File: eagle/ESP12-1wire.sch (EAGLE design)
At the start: 15 parts, among them IC1 LF33CDT, J1 22-05-7038-03, J2 22-05-7038-03, J3 22-05-7038-03, J4 22-05-7048-04

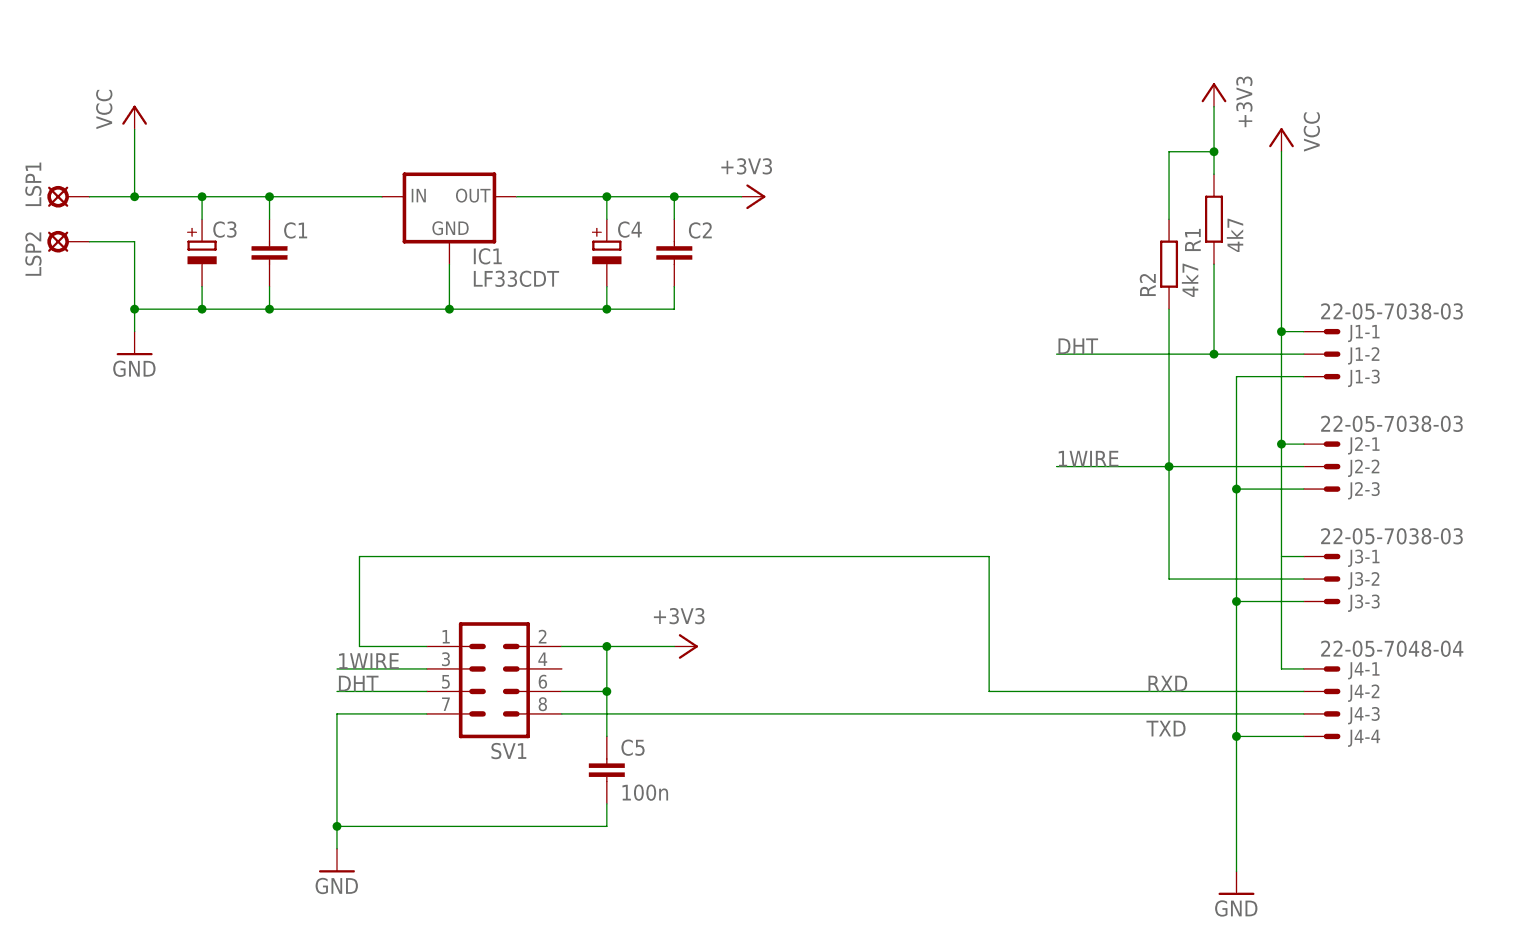
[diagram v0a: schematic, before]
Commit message: new version with ESP-12 module
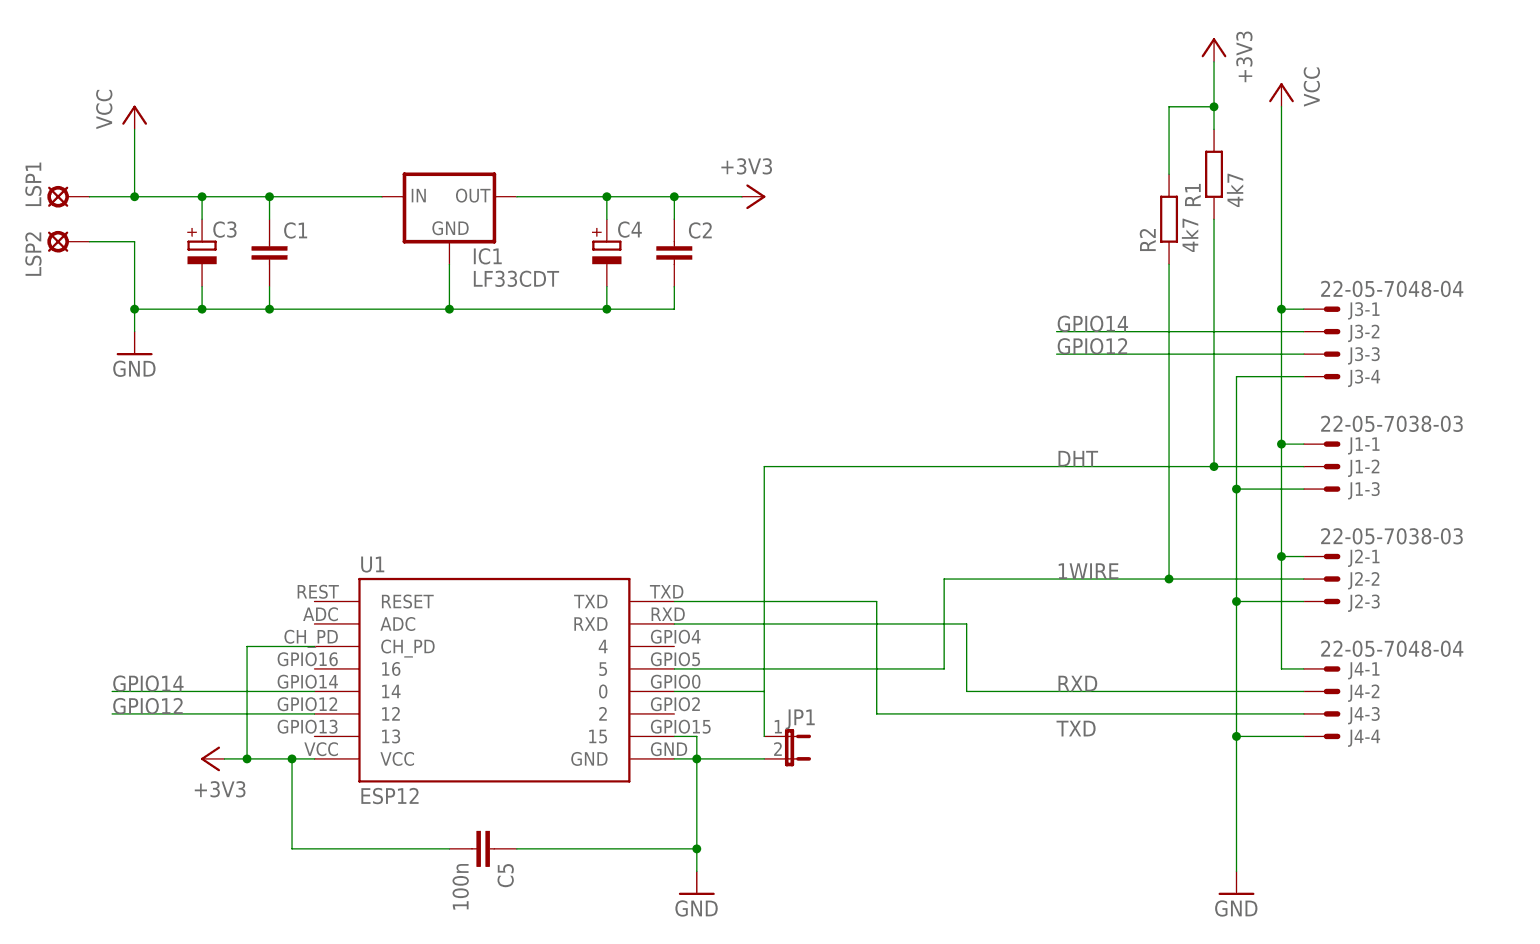
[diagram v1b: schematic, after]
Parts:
- removed SV1: (no value), con-lstb:MA04-2
- added JP1: (no value), jumper:JP1E
- added U1: ESP12, ESP:ESP12
- J3: value 22-05-7038-03 -> 22-05-7048-04; device con-molex:22-05-7038-03 -> con-molex:22-05-7048-04
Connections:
- new net GPIO12: J3-3.S, U1.12
- new net GPIO14: J3-2.S, U1.14
- net +3V3: now also C5.2, U1.CH_PD, U1.VCC; no longer C5.1, SV1.2, SV1.6
- net 1WIRE: now also U1.5; no longer J3-2.S, SV1.3
- net DHT: now also JP1.1, U1.0; no longer SV1.5
- net GND: now also C5.1, J3-4.S, JP1.2, U1.15, U1.GND; no longer C5.2, J3-3.S, SV1.7
- net RXD: now also U1.RXD; no longer SV1.1
- net TXD: now also U1.TXD; no longer SV1.8
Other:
- moved on the sheet: C5, J1-1, J1-2, J1-3, J2-1, J2-2, J2-3, J3-1, J3-2, J3-3, R1, R2
